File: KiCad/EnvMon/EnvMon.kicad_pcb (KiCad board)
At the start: 2 copper layers, 7 parts, among them Q1 2N4401, SW1 SW_DIP_x01, U1 DHT11, U2 XIAO-ESP32-S3-SMD, U3 ER_OLEDM0.91_1x-I2C

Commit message: Update schematic and PCB slightly
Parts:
- SW1: footprint Button_Switch_THT:SW_XKB_DM1-16UP-1 -> Button_Switch_THT:SW_Tactile_Straight_KSA0Axx1LFTR
- U3: value ER_OLEDM0.91_1x-I2C -> 0.91" I2C OLED
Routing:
- net Net-(Q1-E): track 52.3 -> 50.8 mm

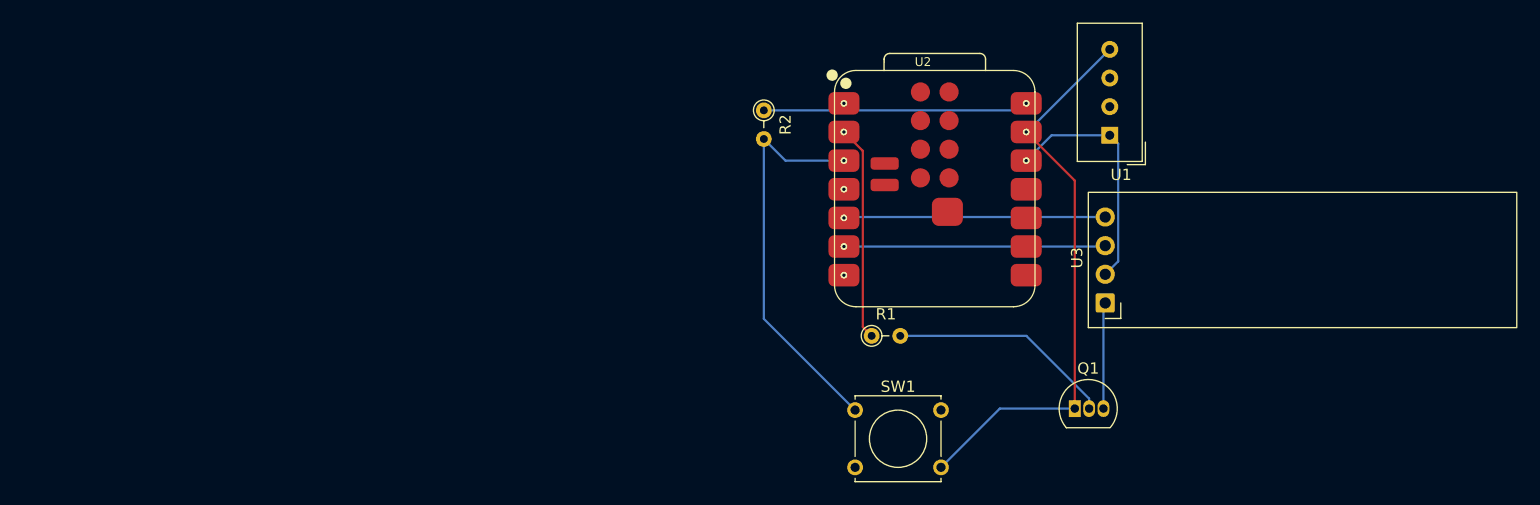
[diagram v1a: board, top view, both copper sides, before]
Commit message: Further KiCAD updates
Not actually using this since went with a prototyping breadboard in the
end, but :shrug:
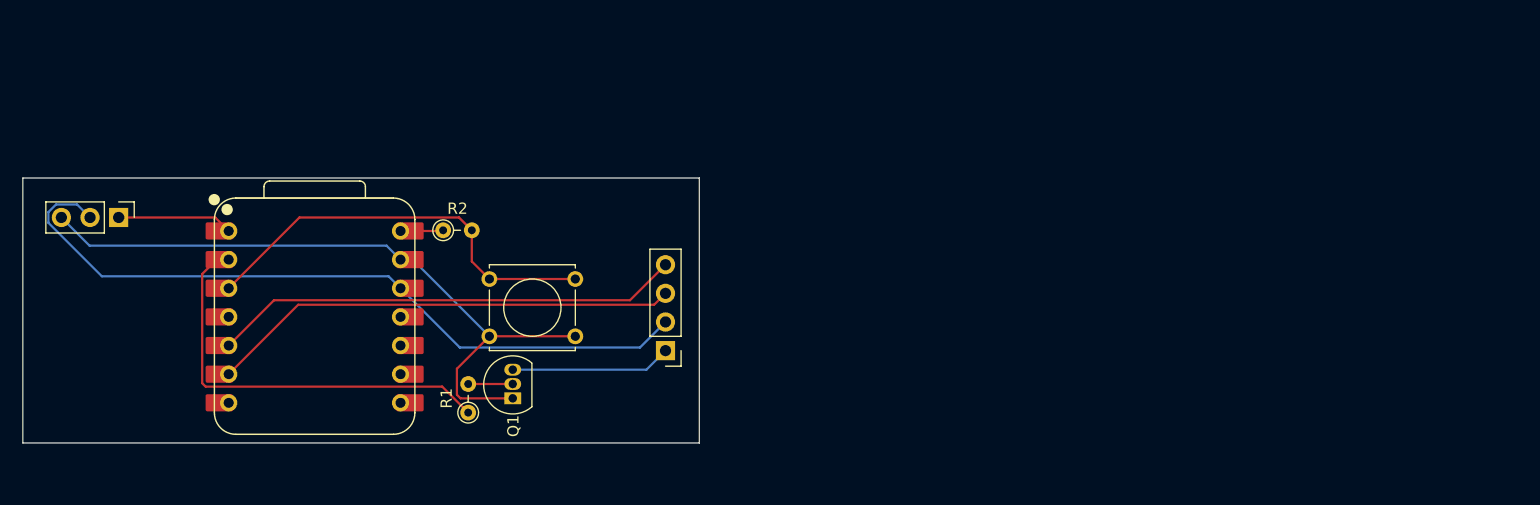
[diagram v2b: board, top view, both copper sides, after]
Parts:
- U1: value DHT11 -> XIAO-ESP32-S3; footprint Sensor:Aosong_DHT11_5.5x12.0_P2.54mm -> Seeed_Studio_XIAO_Series:XIAO-ESP32-S3-DIP
- U2: value XIAO-ESP32-S3-SMD -> DHT11; footprint Seeed_Studio_XIAO_Series:XIAO-ESP32-S3-SMD -> Connector_PinHeader_2.54mm:PinHeader_1x03_P2.54mm_Vertical
- U3: footprint Display:ER_OLEDM0.91_1x-I2C -> Connector_PinHeader_2.54mm:PinHeader_1x04_P2.54mm_Vertical
- moved U1 72.3 mm to (125.4, 85.8), turned to 90 degrees
- moved U2 64.0 mm to (108.0, 77.0), turned to -90 degrees
- moved Q1 49.9 mm to (142.9, 93.0), turned to 90 degrees
- moved U3 39.2 mm to (156.5, 88.8), turned to 180 degrees
- moved R1 36.4 mm to (139.0, 94.3), turned to 90 degrees
- moved SW1 34.5 mm to (140.9, 82.5)
- moved R2 30.4 mm to (136.8, 78.1), turned to 0 degrees
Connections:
- R1 pad 1: Net-(U2-D1) -> Net-(U1-D1)
- R2 pad 1: Net-(U2-VBUS) -> Net-(U1-VBUS)
- R2 pad 2: Net-(U2-D2) -> Net-(U1-D2)
- SW1 pad 1: Net-(U2-D2) -> Net-(U1-D2)
- U1 pad 1: Net-(U1-VDD) -> Net-(U1-D0)
- U1 pad 2: Net-(U1-DATA) -> Net-(U1-D1)
- U1 pad 3: unconnected-(U1-NC-Pad3) -> Net-(U1-D2)
- U1 pad 4: Net-(Q1-E) -> unconnected-(U1-D3-Pad4)
- U2 pad 1: Net-(U1-DATA) -> Net-(U1-D0)
- U2 pad 2: Net-(U2-D1) -> Net-(U1-3V3_OUT)
- U2 pad 3: Net-(U2-D2) -> Net-(Q1-E)
- U3 pad 2: Net-(U1-VDD) -> Net-(U1-3V3_OUT)
- U3 pad 3: Net-(U2-D5) -> Net-(U1-D5)
- U3 pad 4: Net-(U2-D4) -> Net-(U1-D4)
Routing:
- net Net-(U1-3V3_OUT): track 0.00 -> 65.6 mm
- net Net-(U1-D4): track 0.00 -> 41.7 mm
- net Net-(U1-D5): track 0.00 -> 41.7 mm
- net Net-(U1-D1): track 0.00 -> 37.2 mm
- net Net-(U1-D2): track 0.00 -> 37.2 mm
- net Net-(U2-D2): track 35.3 -> 0.00 mm, vias 1 -> 0
- net Net-(U2-D4): track 23.9 -> 0.00 mm, vias 1 -> 0
- net Net-(U2-VBUS): track 23.5 -> 0.00 mm, vias 1 -> 0
- net Net-(U2-D5): track 23.2 -> 0.00 mm, vias 1 -> 0
- net Net-(U1-VDD): track 21.5 -> 0.00 mm, vias 1 -> 0
- net Net-(U2-D1): track 19.1 -> 0.00 mm, vias 1 -> 0
- net Net-(Q1-B): track 19.9 -> 3.95 mm
- net Net-(Q1-E): track 50.8 -> 61.4 mm, vias 1 -> 0
- net Net-(U1-D0): track 0.00 -> 10.3 mm
- net Net-(Q1-C): track 9.44 -> 14.3 mm
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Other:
- board outline added: 60 x 23.5 mm
